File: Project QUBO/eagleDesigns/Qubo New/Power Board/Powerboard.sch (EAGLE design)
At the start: 34 parts, among them IC1 PCF8574T, U1 UEI15, U2 TSR2-2450

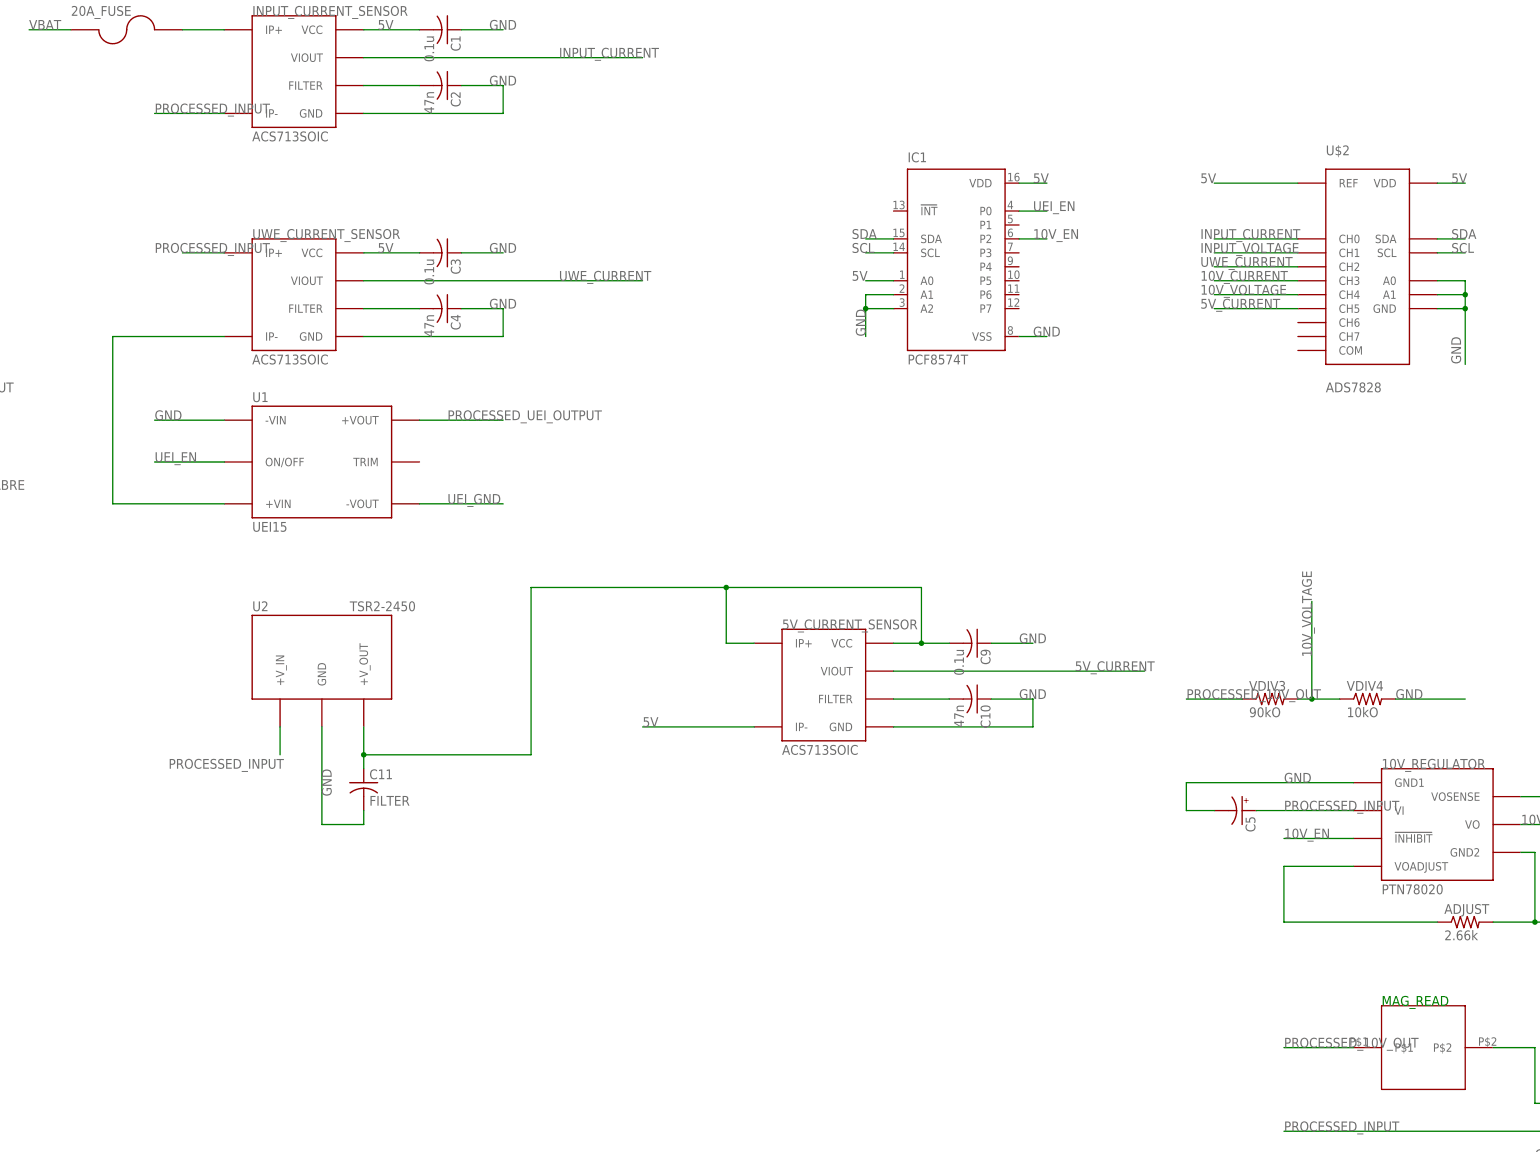
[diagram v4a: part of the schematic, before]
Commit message: misc
some small relabling of a board or two and I retrieved a fixed version of the formerly broken arm board
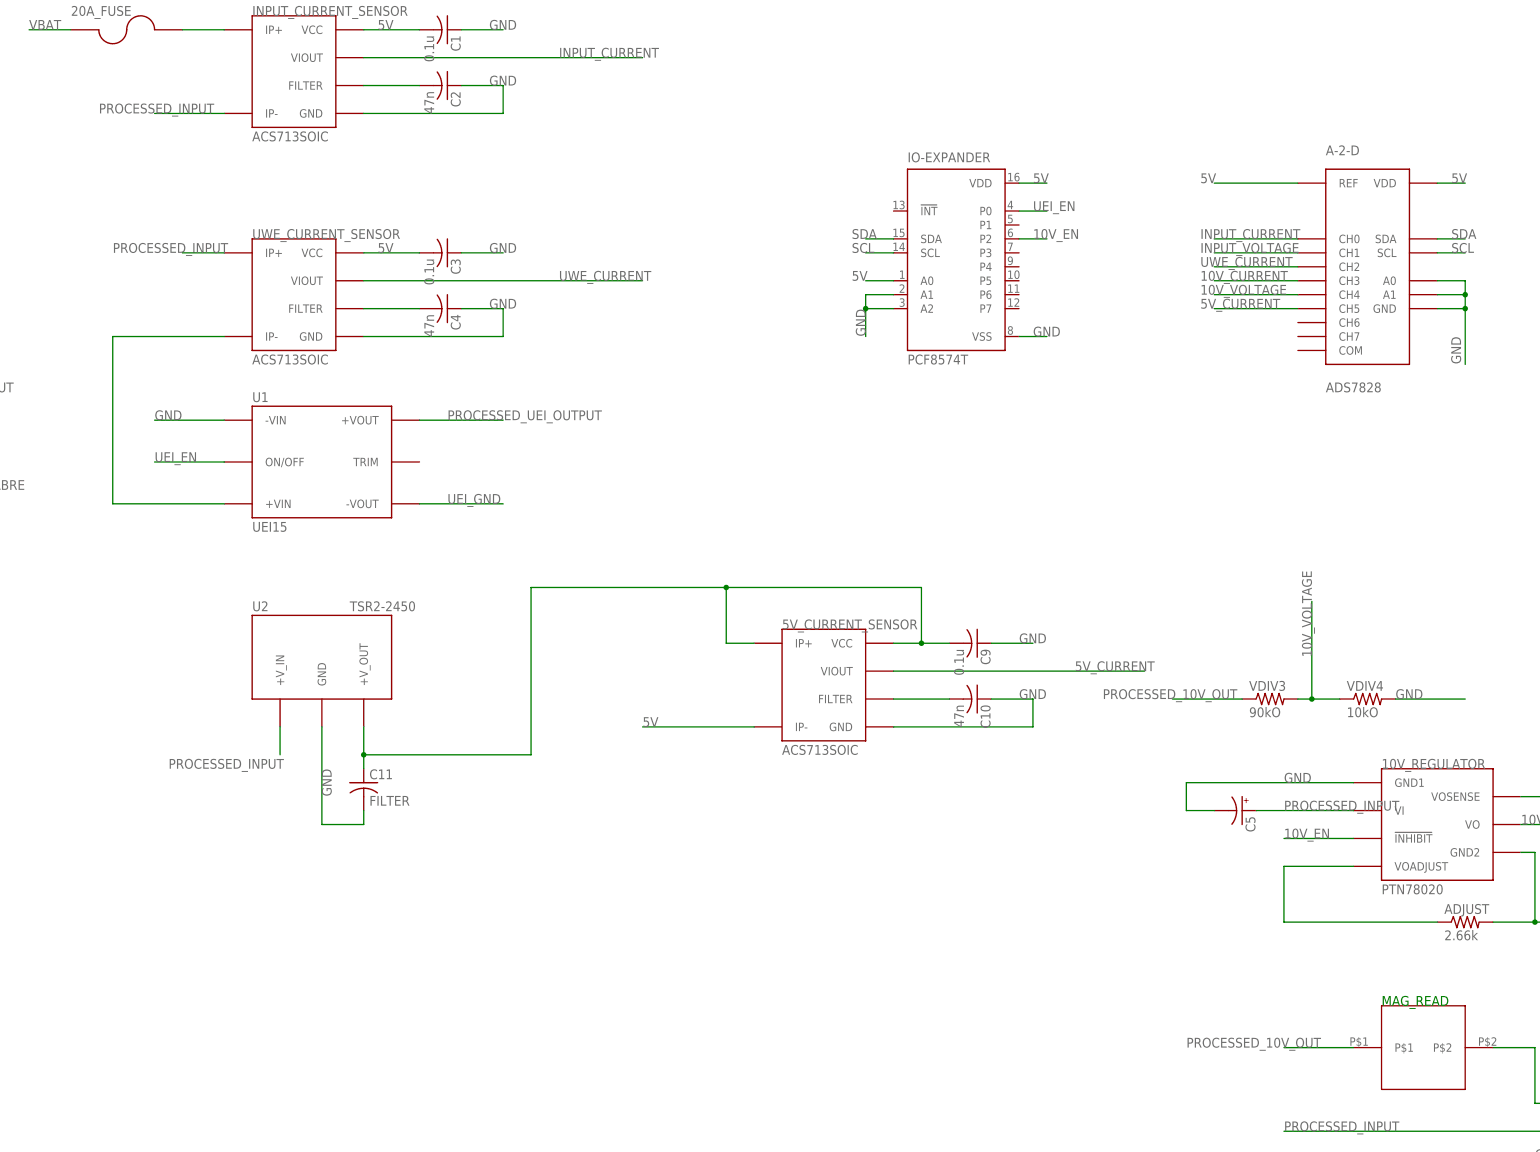
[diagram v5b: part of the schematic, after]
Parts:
- renumbered IC1 to IO-EXPANDER, U$2 to A-2-D
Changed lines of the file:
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@@
 <part name="U$1" library="TE" deviceset="KUHP-5XX1-XX" device=""/>
 <part name="BATTERY_LINE_OUT" library="molex" deviceset="KK254_VERT_2PIN" device="&quot;&quot;"/>
-<part name="U$2" library="texas" deviceset="ADS7828" device=""/>
+<part name="A-2-D" library="texas" deviceset="ADS7828" device=""/>
 <part name="UWE_CURRENT_SENSOR" library="allegro" deviceset="ACS713" device="SOIC"/>
 <part name="C3" library="resistor" deviceset="C-US" device="C0805" value="0.1u"/>
@@
 <part name="VDIV3" library="resistor" deviceset="R-US_" device="R0805" value="90kO"/>
 <part name="VDIV4" library="resistor" deviceset="R-US_" device="R0805" value="10kO"/>
-<part name="IC1" library="texas" deviceset="PCF8574" device="T"/>
+<part name="IO-EXPANDER" library="texas" deviceset="PCF8574" device="T"/>
 <part name="5V_CURRENT_SENSOR" library="allegro" deviceset="ACS713" device="SOIC"/>
 <part name="C9" library="resistor" deviceset="C-US" device="C0805" value="0.1u"/>
@@
 <instance part="U$1" gate="G$1" x="119.38" y="-127"/>
 <instance part="BATTERY_LINE_OUT" gate="U1" x="139.7" y="-7.62"/>
-<instance part="U$2" gate="G$1" x="71.12" y="30.48"/>
+<instance part="A-2-D" gate="G$1" x="71.12" y="30.48"/>
 <instance part="UWE_CURRENT_SENSOR" gate="G$1" x="-124.46" y="25.4"/>
 <instance part="C3" gate="G$1" x="-96.52" y="33.02" rot="R270"/>
@@
 <instance part="VDIV3" gate="G$1" x="53.34" y="-48.26"/>
 <instance part="VDIV4" gate="G$1" x="71.12" y="-48.26"/>
-<instance part="IC1" gate="G$1" x="-5.08" y="33.02"/>
+<instance part="IO-EXPANDER" gate="G$1" x="-5.08" y="33.02"/>
 <instance part="5V_CURRENT_SENSOR" gate="G$1" x="-27.94" y="-45.72"/>
 <instance part="C9" gate="G$1" x="0" y="-38.1" rot="R270"/>
@@
 </segment>
 <segment>
-<pinref part="U$2" gate="G$1" pin="A0"/>
+<pinref part="A-2-D" gate="G$1" pin="A0"/>
 <wire x1="83.82" y1="27.94" x2="88.9" y2="27.94" width="0.1524" layer="91"/>
 <wire x1="88.9" y1="27.94" x2="88.9" y2="25.4" width="0.1524" layer="91"/>
-<pinref part="U$2" gate="G$1" pin="A1"/>
+<pinref part="A-2-D" gate="G$1" pin="A1"/>
 <wire x1="88.9" y1="25.4" x2="88.9" y2="22.86" width="0.1524" layer="91"/>
 <wire x1="88.9" y1="22.86" x2="88.9" y2="12.7" width="0.1524" layer="91"/>
 <wire x1="83.82" y1="25.4" x2="88.9" y2="25.4" width="0.1524" layer="91"/>
 <junction x="88.9" y="25.4"/>
-<pinref part="U$2" gate="G$1" pin="GND"/>
+<pinref part="A-2-D" gate="G$1" pin="GND"/>
 <wire x1="83.82" y1="22.86" x2="88.9" y2="22.86" width="0.1524" layer="91"/>
 <junction x="88.9" y="22.86"/>
@@
 </segment>
 <segment>
-<pinref part="IC1" gate="G$1" pin="VSS"/>
+<pinref part="IO-EXPANDER" gate="G$1" pin="VSS"/>
 <wire x1="7.62" y1="17.78" x2="12.7" y2="17.78" width="0.1524" layer="91"/>
 <label x="10.16" y="17.78" size="1.778" layer="95"/>
 </segment>
 <segment>
-<pinref part="IC1" gate="G$1" pin="A1"/>
+<pinref part="IO-EXPANDER" gate="G$1" pin="A1"/>
 <wire x1="-15.24" y1="25.4" x2="-20.32" y2="25.4" width="0.1524" layer="91"/>
 <wire x1="-20.32" y1="25.4" x2="-20.32" y2="22.86" width="0.1524" layer="91"/>
-<pinref part="IC1" gate="G$1" pin="A2"/>
+<pinref part="IO-EXPANDER" gate="G$1" pin="A2"/>
 <wire x1="-20.32" y1="22.86" x2="-20.32" y2="17.78" width="0.1524" layer="91"/>
 <wire x1="-15.24" y1="22.86" x2="-20.32" y2="22.86" width="0.1524" layer="91"/>
@@
 </segment>
 <segment>
-<pinref part="U$2" gate="G$1" pin="REF"/>
+<pinref part="A-2-D" gate="G$1" pin="REF"/>
 <wire x1="58.42" y1="45.72" x2="43.18" y2="45.72" width="0.1524" layer="91"/>
 <label x="40.64" y="45.72" size="1.778" layer="95"/>
 </segment>
 <segment>
-<pinref part="U$2" gate="G$1" pin="VDD"/>
+<pinref part="A-2-D" gate="G$1" pin="VDD"/>
 <wire x1="83.82" y1="45.72" x2="88.9" y2="45.72" width="0.1524" layer="91"/>
 <label x="86.36" y="45.72" size="1.778" layer="95"/>
 </segment>
 <segment>
-<pinref part="IC1" gate="G$1" pin="VDD"/>
+<pinref part="IO-EXPANDER" gate="G$1" pin="VDD"/>
 <label x="10.16" y="45.72" size="1.778" layer="95"/>
 <wire x1="7.62" y1="45.72" x2="12.7" y2="45.72" width="0.1524" layer="91"/>
@@
 </segment>
 <segment>
-<pinref part="IC1" gate="G$1" pin="A0"/>
+<pinref part="IO-EXPANDER" gate="G$1" pin="A0"/>
 <wire x1="-15.24" y1="27.94" x2="-20.32" y2="27.94" width="0.1524" layer="91"/>
 <label x="-22.86" y="27.94" size="1.778" layer="95"/>
@@
 <pinref part="INPUT_CURRENT_SENSOR" gate="G$1" pin="IP-"/>
 <wire x1="-137.16" y1="58.42" x2="-149.86" y2="58.42" width="0.1524" layer="91"/>
-<label x="-149.86" y="58.42" size="1.778" layer="95"/>
+<label x="-160.02" y="58.42" size="1.778" layer="95"/>
 </segment>
 <segment>
@@
 <pinref part="UWE_CURRENT_SENSOR" gate="G$1" pin="IP+"/>
 <wire x1="-144.78" y1="33.02" x2="-137.16" y2="33.02" width="0.1524" layer="91"/>
-<label x="-149.86" y="33.02" size="1.778" layer="95"/>
+<label x="-157.48" y="33.02" size="1.778" layer="95"/>
 </segment>
 <segment>
@@
 <net name="UEI_EN" class="0">
 <segment>
-<pinref part="IC1" gate="G$1" pin="P0"/>
+<pinref part="IO-EXPANDER" gate="G$1" pin="P0"/>
 <wire x1="7.62" y1="40.64" x2="12.7" y2="40.64" width="0.1524" layer="91"/>
 <label x="10.16" y="40.64" size="1.778" layer="95"/>
@@
 </segment>
 <segment>
-<pinref part="U$2" gate="G$1" pin="CH1"/>
+<pinref part="A-2-D" gate="G$1" pin="CH1"/>
 <wire x1="58.42" y1="33.02" x2="43.18" y2="33.02" width="0.1524" layer="91"/>
 <label x="40.64" y="33.02" size="1.778" layer="95"/>
@@
 </segment>
 <segment>
-<pinref part="IC1" gate="G$1" pin="P2"/>
+<pinref part="IO-EXPANDER" gate="G$1" pin="P2"/>
 <wire x1="7.62" y1="35.56" x2="12.7" y2="35.56" width="0.1524" layer="91"/>
 <label x="10.16" y="35.56" size="1.778" layer="95"/>
@@
 <pinref part="MAGREAD" gate="G$1" pin="P$1"/>
 <wire x1="68.58" y1="-111.76" x2="55.88" y2="-111.76" width="0.1524" layer="91"/>
-<label x="55.88" y="-111.76" size="1.778" layer="95"/>
+<label x="38.1" y="-111.76" size="1.778" layer="95"/>
 </segment>
 <segment>
 <pinref part="VDIV3" gate="G$1" pin="1"/>
-<wire x1="48.26" y1="-48.26" x2="38.1" y2="-48.26" width="0.1524" layer="91"/>
-<label x="38.1" y="-48.26" size="1.778" layer="95"/>
+<wire x1="48.26" y1="-48.26" x2="35.56" y2="-48.26" width="0.1524" layer="91"/>
+<label x="22.86" y="-48.26" size="1.778" layer="95"/>
 </segment>
 </net>
@@
 </segment>
 <segment>
-<pinref part="U$2" gate="G$1" pin="CH2"/>
+<pinref part="A-2-D" gate="G$1" pin="CH2"/>
 <wire x1="58.42" y1="30.48" x2="43.18" y2="30.48" width="0.1524" layer="91"/>
 <label x="40.64" y="30.48" size="1.778" layer="95"/>
@@
 </segment>
 <segment>
-<pinref part="U$2" gate="G$1" pin="CH0"/>
+<pinref part="A-2-D" gate="G$1" pin="CH0"/>
 <wire x1="58.42" y1="35.56" x2="43.18" y2="35.56" width="0.1524" layer="91"/>
 <label x="40.64" y="35.56" size="1.778" layer="95"/>
@@
 </segment>
 <segment>
-<pinref part="U$2" gate="G$1" pin="CH3"/>
+<pinref part="A-2-D" gate="G$1" pin="CH3"/>
 <wire x1="58.42" y1="27.94" x2="43.18" y2="27.94" width="0.1524" layer="91"/>
 <label x="40.64" y="27.94" size="1.778" layer="95"/>
@@
 <net name="SDA" class="0">
 <segment>
-<pinref part="U$2" gate="G$1" pin="SDA"/>
+<pinref part="A-2-D" gate="G$1" pin="SDA"/>
 <wire x1="83.82" y1="35.56" x2="88.9" y2="35.56" width="0.1524" layer="91"/>
 <label x="86.36" y="35.56" size="1.778" layer="95"/>
@@
 </segment>
 <segment>
-<pinref part="IC1" gate="G$1" pin="SDA"/>
+<pinref part="IO-EXPANDER" gate="G$1" pin="SDA"/>
 <wire x1="-15.24" y1="35.56" x2="-20.32" y2="35.56" width="0.1524" layer="91"/>
 <label x="-22.86" y="35.56" size="1.778" layer="95"/>
@@
 <net name="SCL" class="0">
 <segment>
-<pinref part="U$2" gate="G$1" pin="SCL"/>
+<pinref part="A-2-D" gate="G$1" pin="SCL"/>
 <wire x1="83.82" y1="33.02" x2="88.9" y2="33.02" width="0.1524" layer="91"/>
 <label x="86.36" y="33.02" size="1.778" layer="95"/>
@@
 </segment>
 <segment>
-<pinref part="IC1" gate="G$1" pin="SCL"/>
+<pinref part="IO-EXPANDER" gate="G$1" pin="SCL"/>
 <wire x1="-15.24" y1="33.02" x2="-20.32" y2="33.02" width="0.1524" layer="91"/>
 <label x="-22.86" y="33.02" size="1.778" layer="95"/>
@@
 </segment>
 <segment>
-<pinref part="U$2" gate="G$1" pin="CH4"/>
+<pinref part="A-2-D" gate="G$1" pin="CH4"/>
 <wire x1="58.42" y1="25.4" x2="43.18" y2="25.4" width="0.1524" layer="91"/>
 <label x="40.64" y="25.4" size="1.778" layer="95"/>
@@
 </segment>
 <segment>
-<pinref part="U$2" gate="G$1" pin="CH5"/>
+<pinref part="A-2-D" gate="G$1" pin="CH5"/>
 <wire x1="58.42" y1="22.86" x2="43.18" y2="22.86" width="0.1524" layer="91"/>
 <label x="40.64" y="22.86" size="1.778" layer="95"/>
